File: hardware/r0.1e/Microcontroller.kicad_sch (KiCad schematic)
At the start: 95 parts, among them J10 UART, J2 USB_C, J3 OLED, J8 +12V, J9 STLink, Q4 IRLML2244, Q5 MMBT3904, SW1 Button Up, SW2 Button Down, SW3 Reset, SW4 Button Escape, SW5 Button Left, SW6 Button Enter, SW7 Button Right, SW8 Button Power, U10 STM32F405RGTx, U11 TPS7A2033, U2 TP6841S6, U3 USBLC6-2, X1 12 MHz TCXO, Y1 8 MHz

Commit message: Updated JLC fabrication files
Replaced reset button and BSS138 FETs
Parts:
- SW3: LCSC Part # C589193 -> C221895; MPN ST-1185SE -> PTS810SJG250SMTRLFS
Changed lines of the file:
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@@
       (effects (font (size 1.27 1.27)) hide)
     )
-    (property "MPN" "ST-1185SE" (at 240.03 110.49 0)
+    (property "MPN" "PTS810SJG250SMTRLFS" (at 240.03 110.49 0)
       (effects (font (size 1.27 1.27)) hide)
     )
-    (property "LCSC Part #" "C589193" (at 240.03 110.49 0)
+    (property "LCSC Part #" "C221895" (at 240.03 110.49 0)
       (effects (font (size 1.27 1.27)) hide)
     )

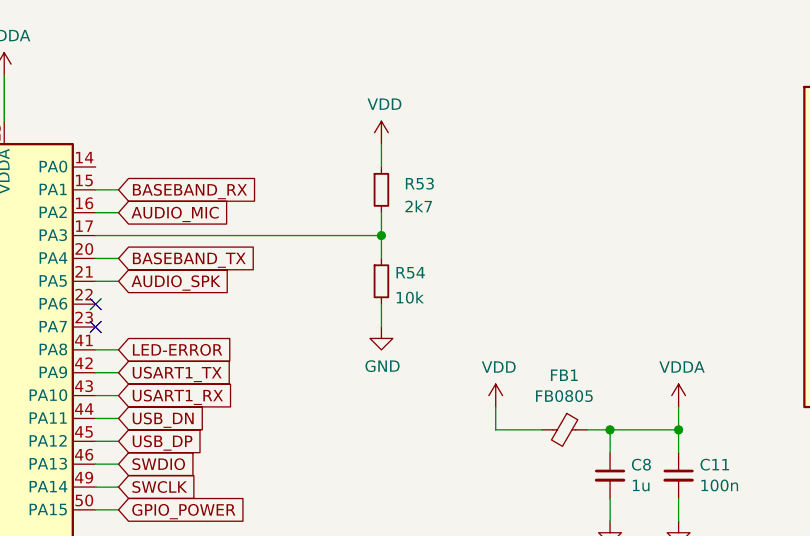
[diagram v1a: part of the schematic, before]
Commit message: Fix R53 to 0R link for 3V3 pullup, update BOM for R31 and R53
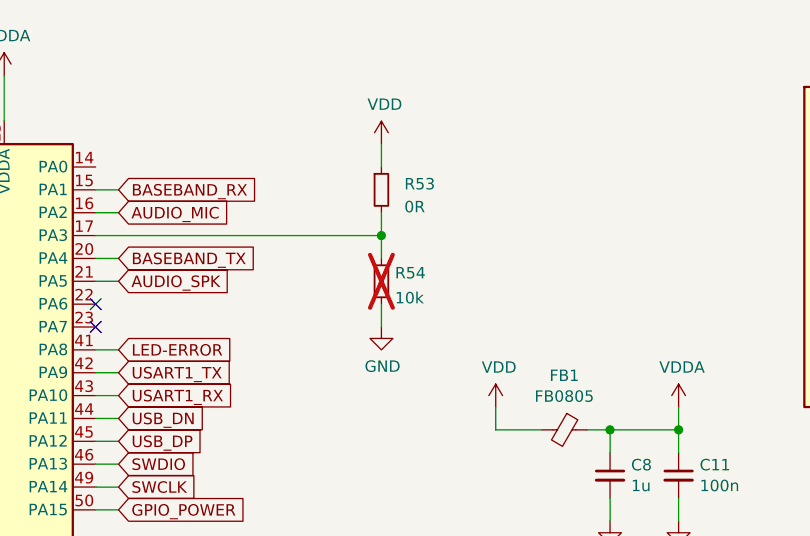
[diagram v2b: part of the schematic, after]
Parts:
- R53: value 2k7 -> 0R
- R54: now not fitted; now left out of the parts list
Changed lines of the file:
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@@
       (effects (font (size 1.27 1.27)) (justify left))
     )
-    (property "Value" "2k7" (at 143.51 33.655 0)
+    (property "Value" "0R" (at 143.51 33.655 0)
       (effects (font (size 1.27 1.27)) (justify left))
     )
@@
   )
   (symbol (lib_id "pkl_device:pkl_R_Small") (at 140.97 41.91 0) (unit 1)
-    (in_bom yes) (on_board yes) (dnp no) (fields_autoplaced)
+    (in_bom no) (on_board no) (dnp yes) (fields_autoplaced)
     (property "Reference" "R54" (at 142.4687 41.0015 0)
       (effects (font (size 1.27 1.27)) (justify left))

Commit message: Revert "Merge remote-tracking branch 'origin/main' into main"
This reverts commit 2e86e4066111431c9dfb042395a1f17233de766b, reversing
changes made to 3880e228021d6506ff5a6ac426a77f17ffdc8eb9.
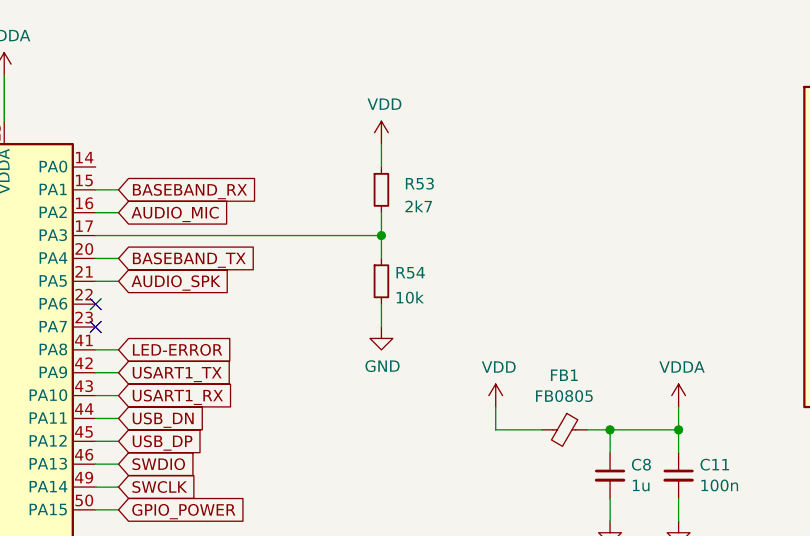
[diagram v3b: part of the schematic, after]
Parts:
- R53: value 0R -> 2k7
- R54: now fitted; now in the parts list
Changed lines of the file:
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@@
       (effects (font (size 1.27 1.27)) (justify left))
     )
-    (property "Value" "0R" (at 143.51 33.655 0)
+    (property "Value" "2k7" (at 143.51 33.655 0)
       (effects (font (size 1.27 1.27)) (justify left))
     )
@@
   )
   (symbol (lib_id "pkl_device:pkl_R_Small") (at 140.97 41.91 0) (unit 1)
-    (in_bom no) (on_board no) (dnp yes) (fields_autoplaced)
+    (in_bom yes) (on_board yes) (dnp no) (fields_autoplaced)
     (property "Reference" "R54" (at 142.4687 41.0015 0)
       (effects (font (size 1.27 1.27)) (justify left))

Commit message: Fix KC1AWV original fixes
Fix schematic and PCB layout. Populate R53 with 0R and update BOM to include R31 change
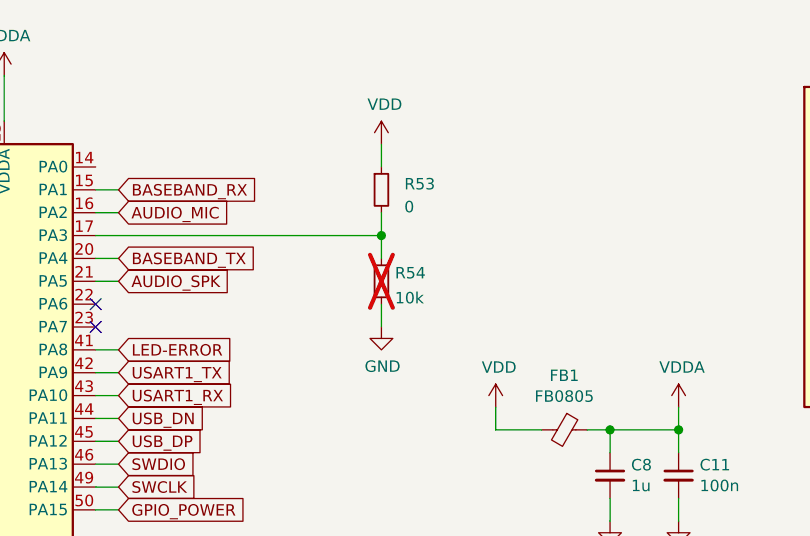
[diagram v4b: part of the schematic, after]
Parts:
- R53: value 2k7 -> 0
- R54: now not fitted
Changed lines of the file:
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@@
       (effects (font (size 1.27 1.27)) (justify left))
     )
-    (property "Value" "2k7" (at 143.51 33.655 0)
+    (property "Value" "0" (at 143.51 33.655 0)
       (effects (font (size 1.27 1.27)) (justify left))
     )
@@
   )
   (symbol (lib_id "pkl_device:pkl_R_Small") (at 140.97 41.91 0) (unit 1)
-    (in_bom yes) (on_board yes) (dnp no) (fields_autoplaced)
+    (in_bom yes) (on_board yes) (dnp yes) (fields_autoplaced)
     (property "Reference" "R54" (at 142.4687 41.0015 0)
       (effects (font (size 1.27 1.27)) (justify left))
